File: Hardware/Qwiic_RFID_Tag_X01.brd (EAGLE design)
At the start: 112.5 x 103.6 mm, 294 parts, among them J1 Qwiic, J10 Qwiic, J11 Qwiic, J13 Qwiic, J14 Qwiic, J16 Qwiic, J17 Qwiic, J2 Qwiic, J4 Qwiic, J5 Qwiic, J7 Qwiic, J8 Qwiic, U1 ST25DV64KC, U2 ST25DV64KC, U3 ST25DV64KC, U4 ST25DV64KC, U5 ST25DV64KC, U6 ST25DV64KC

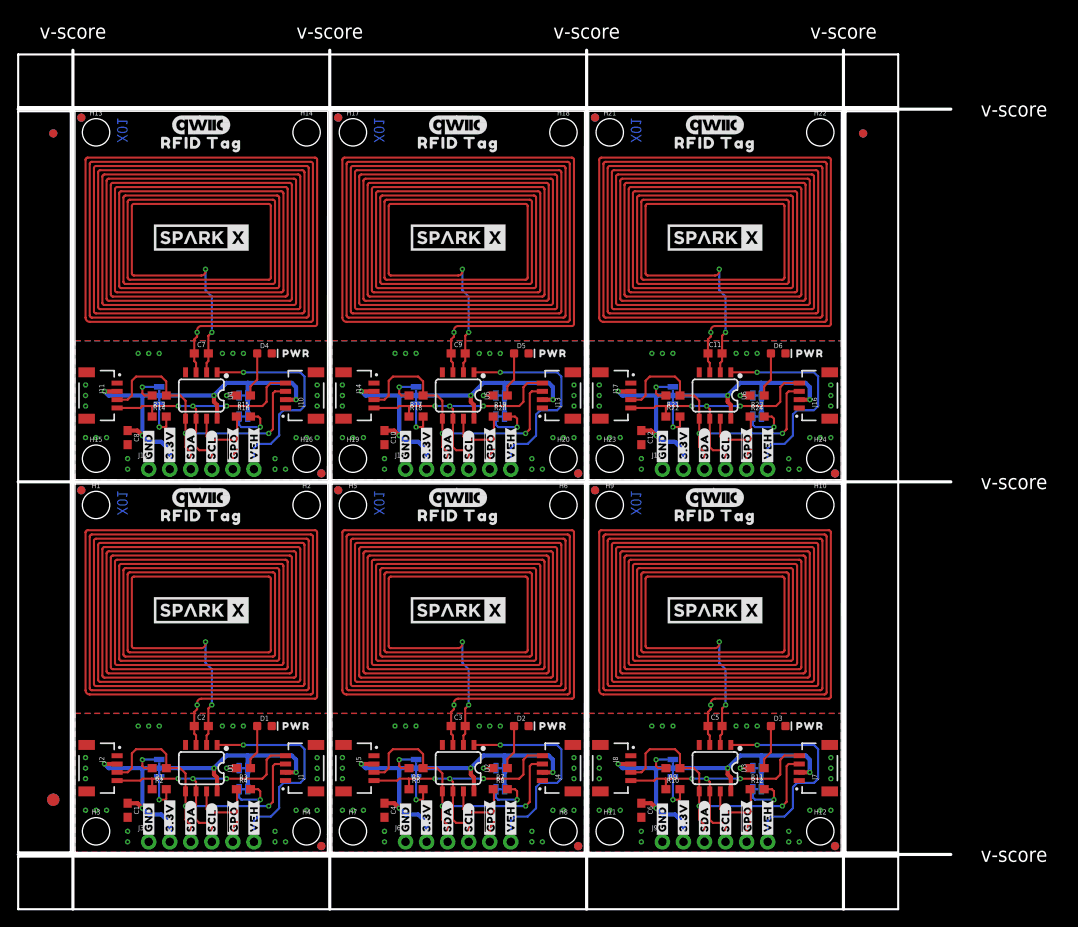
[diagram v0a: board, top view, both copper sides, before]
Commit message: Renamed file to reflect version. Added PCB version to bottom silk.
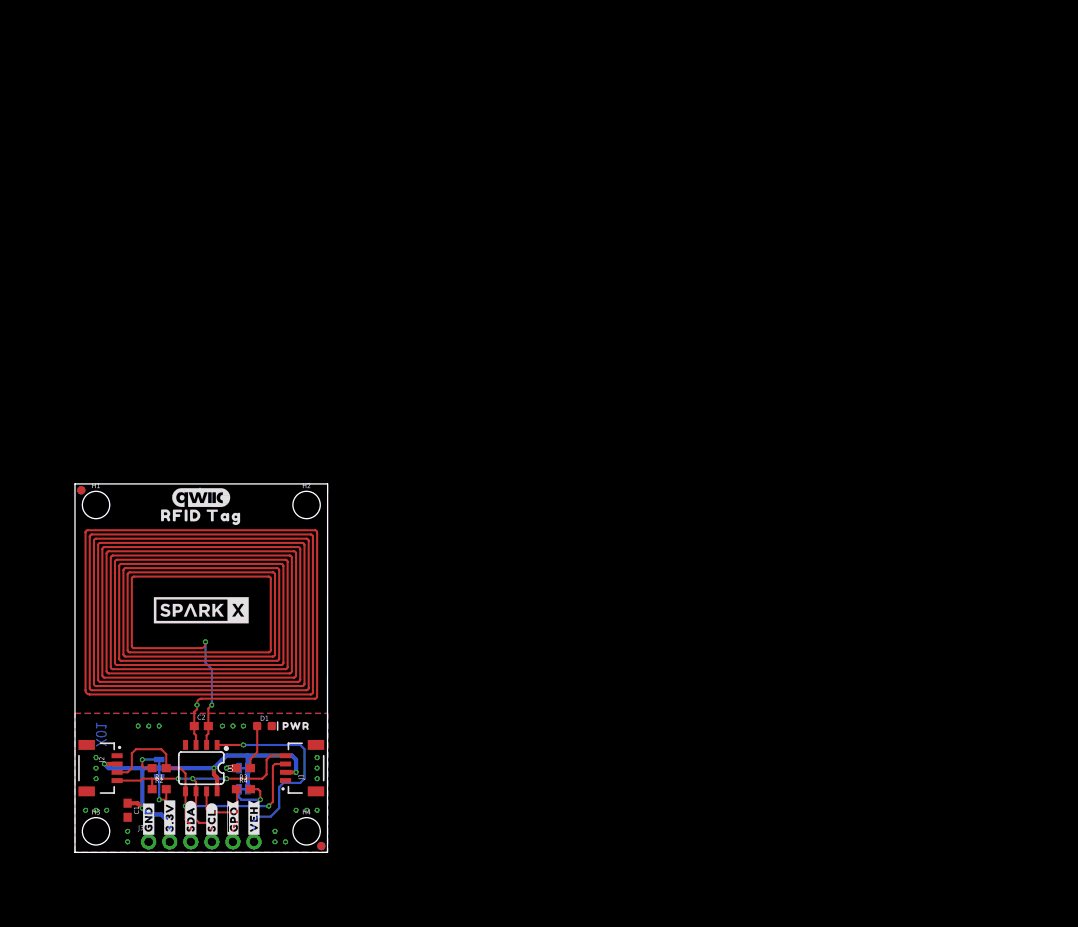
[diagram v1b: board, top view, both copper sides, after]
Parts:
- removed C10, C12, C4, C6, C8: 0.1uF, SparkFun-Capacitors:0603
- removed C11, C3, C5, C7, C9: 4.7pF, SparkFun-Capacitors:0603
- removed D2, D3, D4, D5, D6: RED, SparkFun-LED:LED-0603
- removed E$1, E$2, E$3, E$4: (no value), SparkFun-Aesthetics:FIDUCIAL-1X2
- removed E$5, E$6: (no value), SparkFun-Retired:FIDUCIAL-1.5X3
- removed FD10, FD11, FD12, FD13, FD14, FD15, FD16, FD17, FD18, FD19, FD20, FD21, FD22, FD23, FD24, FD5, FD6, FD7, FD8, FD9: FIDUCIAL1X2, SparkFun-Aesthetics:FIDUCIAL-1X2
- removed FRAME2, FRAME3, FRAME4, FRAME5, FRAME6: FRAME-LETTERNO_PACKAGE, SparkFun-Aesthetics:DUMMY
- removed H10, H11, H12, H13, H14, H15, H16, H17, H18, H19, H20, H21, H22, H23, H24, H5, H6, H7, H8, H9: STAND-OFF, SparkFun-Hardware:STAND-OFF
- removed J10, J11, J13, J14, J16, J17, J4, J5, J7, J8: Qwiic, SparkFun-Connectors:JST04_1MM_RA
- removed J12, J15, J18, J6, J9: (no value), SparkFun-Connectors:1X06_NO_SILK
- removed JP10, JP13, JP16, JP4, JP7: JUMPER-SMT_3_2-NC_TRACE_SILK, SparkFun-Jumpers:SMT-JUMPER_3_2-NC_TRACE_SILK
- removed JP11, JP12, JP14, JP15, JP17, JP18, JP5, JP6, JP8, JP9: JUMPER-SMT_2_NC_TRACE_SILK, SparkFun-Jumpers:SMT-JUMPER_2_NC_TRACE_SILK
- removed L2, L3, L4, L5, L6: PCB_4UH_INDUCTOR, SparkFun-Coils:PCB_4UH_INDUCTOR
- removed LOGO10, LOGO13, LOGO16, LOGO4, LOGO7: OSHW-LOGOMINI, SparkFun-Aesthetics:OSHW-LOGO-MINI
- removed LOGO11, LOGO12, LOGO14, LOGO15, LOGO17, LOGO18, LOGO5, LOGO6, LOGO8, LOGO9: QWIIC_LOGO_7MM, SparkFun-Aesthetics:QWIIC_7MM
- removed R10, R13, R14, R17, R18, R21, R22, R5, R6, R9: 2.2k, SparkFun-Resistors:0603
- removed R11, R15, R19, R23, R7: 1k, SparkFun-Resistors:0603
- removed R12, R16, R20, R24, R8: 10k, SparkFun-Resistors:0603
- removed U$100, U$110, U$121, U$26, U$37, U$47, U$58, U$68, U$79, U$89: (no value), output:#SDA#5
- removed U$101, U$111, U$122, U$27, U$38, U$48, U$59, U$69, U$80, U$90: (no value), output:#SCL#6
- removed U$102, U$112, U$123, U$28, U$39, U$49, U$60, U$70, U$81, U$91: (no value), output:##GPO##8
- removed U$103, U$113, U$124, U$29, U$40, U$50, U$61, U$71, U$82, U$92: (no value), output:#VEH#7
- removed U$104, U$105, U$125, U$126, U$41, U$42, U$62, U$63, U$83, U$84: (no value), output:RFID_TAG13
- removed U$106, U$107, U$13, U$43, U$44, U$64, U$65, U$85, U$86: SPARKX-LOGO5, SparkX:SPARKX-LARGE
- removed U$108, U$120, U$24, U$36, U$45, U$57, U$66, U$78, U$87, U$99: (no value), output:#3#3V#0
- removed U$109, U$119, U$25, U$35, U$46, U$56, U$67, U$77, U$88, U$98: (no value), output:#GND#4
- removed U$114, U$30, U$51, U$72, U$93: (no value), output:PWR11
- removed U$115, U$31, U$52, U$73, U$94: (no value), output:MADE_IN_THE_USA27
- removed U$116, U$32, U$53, U$74, U$95: (no value), output:#I2C#11
- removed U$117, U$33, U$54, U$75, U$96: (no value), output:##GPO##9
- removed U$118, U$34, U$55, U$76, U$97: (no value), output:#LED#10
- removed U2, U3, U4, U5, U6: ST25DV64KC, SparkFun-RF:SO08
- U$10: value SPARKX-LOGO5 -> (none); device SparkX:SPARKX-LARGE -> numbers:PCB#16329163281
- moved U$10 48.3 mm to (1.27, 11.7), flipped to the bottom, turned to 90 degrees
- moved LOGO1 27.0 mm to (28.7, 15.2)
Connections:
- removed net !GPO!1: J6.5, R8.1, U2.7
- removed net !GPO!2: J9.5, R12.1, U3.7
- removed net !GPO!3: J12.5, R16.1, U4.7
- removed net !GPO!4: J15.5, R20.1, U5.7
- removed net !GPO!5: J18.5, R24.1, U6.7
- removed net 3.3V1: C4.1, J4.2, J5.2, J6.2, JP4.2, JP5.2, JP6.2, U2.8
- removed net 3.3V2: C6.1, J7.2, J8.2, J9.2, JP7.2, JP8.2, JP9.2, U3.8
- removed net 3.3V3: C8.1, J10.2, J11.2, J12.2, JP10.2, JP11.2, JP12.2, U4.8
- removed net 3.3V4: C10.1, J13.2, J14.2, J15.2, JP13.2, JP14.2, JP15.2, U5.8
- removed net 3.3V5: C12.1, J16.2, J17.2, J18.2, JP16.2, JP17.2, JP18.2, U6.8
- removed net AC10: C11.2, L6.IN1, U6.2
- removed net AC11: C11.1, L6.IN2, U6.3
- removed net AC2: C3.2, L2.IN1, U2.2
- removed net AC3: C3.1, L2.IN2, U2.3
- removed net AC4: C5.2, L3.IN1, U3.2
- removed net AC5: C5.1, L3.IN2, U3.3
- removed net AC6: C7.2, L4.IN1, U4.2
- removed net AC7: C7.1, L4.IN2, U4.3
- removed net AC8: C9.2, L5.IN1, U5.2
- removed net AC9: C9.1, L5.IN2, U5.3
- removed net GND1: C4.2, D2.C, J4.1, J5.1, J6.1, U2.4
- removed net GND2: C6.2, D3.C, J7.1, J8.1, J9.1, U3.4
- removed net GND3: C8.2, D4.C, J10.1, J11.1, J12.1, U4.4
- removed net GND4: C10.2, D5.C, J13.1, J14.1, J15.1, U5.4
- removed net GND5: C12.2, D6.C, J16.1, J17.1, J18.1, U6.4
- removed net N$10: JP6.1, R8.2
- removed net N$11: JP7.3, R9.2
- removed net N$12: JP7.1, R10.2
- removed net N$13: JP8.1, R11.2
- removed net N$14: D3.A, R11.1
- removed net N$15: JP9.1, R12.2
- removed net N$16: JP10.3, R13.2
- removed net N$17: JP10.1, R14.2
- removed net N$18: JP11.1, R15.2
- removed net N$19: D4.A, R15.1
- removed net N$20: JP12.1, R16.2
- removed net N$21: JP13.3, R17.2
- removed net N$22: JP13.1, R18.2
- removed net N$23: JP14.1, R19.2
- removed net N$24: D5.A, R19.1
- removed net N$25: JP15.1, R20.2
- removed net N$26: JP16.3, R21.2
- removed net N$27: JP16.1, R22.2
- removed net N$28: JP17.1, R23.2
- removed net N$29: D6.A, R23.1
- removed net N$30: JP18.1, R24.2
- removed net N$6: JP4.3, R5.2
- removed net N$7: JP4.1, R6.2
- removed net N$8: JP5.1, R7.2
- removed net N$9: D2.A, R7.1
- removed net SCL1: J4.4, J5.4, J6.4, R6.1, U2.6
- removed net SCL2: J7.4, J8.4, J9.4, R10.1, U3.6
- removed net SCL3: J10.4, J11.4, J12.4, R14.1, U4.6
- removed net SCL4: J13.4, J14.4, J15.4, R18.1, U5.6
- removed net SCL5: J16.4, J17.4, J18.4, R22.1, U6.6
- removed net SDA1: J4.3, J5.3, J6.3, R5.1, U2.5
- removed net SDA2: J7.3, J8.3, J9.3, R9.1, U3.5
- removed net SDA3: J10.3, J11.3, J12.3, R13.1, U4.5
- removed net SDA4: J13.3, J14.3, J15.3, R17.1, U5.5
- removed net SDA5: J16.3, J17.3, J18.3, R21.1, U6.5
- removed net VEH1: J6.6, U2.1
- removed net VEH2: J9.6, U3.1
- removed net VEH3: J12.6, U4.1
- removed net VEH4: J15.6, U5.1
- removed net VEH5: J18.6, U6.1
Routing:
- net 3.3V5: track 48.7 -> 0.00 mm, vias 4 -> 0
- net 3.3V4: track 48.7 -> 0.00 mm, vias 4 -> 0
- net 3.3V3: track 48.7 -> 0.00 mm, vias 4 -> 0
- net 3.3V2: track 48.7 -> 0.00 mm, vias 4 -> 0
- net 3.3V1: track 48.7 -> 0.00 mm, vias 4 -> 0
- net SDA4: track 37.9 -> 0.00 mm, vias 2 -> 0
- net SDA3: track 37.9 -> 0.00 mm, vias 2 -> 0
- net SDA5: track 37.9 -> 0.00 mm, vias 2 -> 0
- net SDA2: track 37.9 -> 0.00 mm, vias 2 -> 0
- net SDA1: track 37.9 -> 0.00 mm, vias 2 -> 0
- net SCL2: track 33.1 -> 0.00 mm, vias 3 -> 0
- net SCL1: track 33.1 -> 0.00 mm, vias 3 -> 0
- net SCL5: track 33.1 -> 0.00 mm, vias 3 -> 0
- net SCL3: track 33.1 -> 0.00 mm, vias 3 -> 0
- net SCL4: track 33.1 -> 0.00 mm, vias 3 -> 0
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- removed copper zone on layer 1, net GND1
- removed copper zone on layer 16, net GND1
- removed copper zone on layer 1, net GND2
- removed copper zone on layer 16, net GND2
- removed copper zone on layer 1, net GND3
- removed copper zone on layer 16, net GND3
- removed copper zone on layer 1, net GND4
- removed copper zone on layer 16, net GND4
- removed copper zone on layer 1, net GND5
- removed copper zone on layer 16, net GND5
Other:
- board size 112.5 x 103.6 mm -> 30.5 x 44.5 mm
- board text added: "Dimensions in inches"
- board text removed: "v-score"

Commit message: Added production files; updated BOM.
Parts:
- removed U$10: (no value), numbers:PCB#16329163281
- removed U$14: (no value), output:MADE_IN_THE_USA27
- added U$13, U$24: (no value), SER:ST25DV64KC5984
- added U$34: (no value), output:MADE_IN_THE_USA20
- moved U$2 13.5 mm to (15.2, 28.4)
- moved U$12 11.9 mm to (15.2, 40.6)
- moved LOGO3 11.4 mm to (15.2, 31.4)
- moved U$1 1.02 mm to (15.2, 28.2)
- moved LOGO2 0.25 mm to (15.2, 31.6)
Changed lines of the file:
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@@
 <setting verticaltext="up"/>
 </settings>
-<grid distance="0.05" unitdist="inch" unit="inch" style="lines" multiple="1" display="yes" altdistance="0.005" altunitdist="inch" altunit="inch"/>
+<grid distance="0.01" unitdist="inch" unit="inch" style="lines" multiple="1" display="yes" altdistance="0.005" altunitdist="inch" altunit="inch"/>
 <layers>
 <layer number="1" name="Top" color="4" fill="1" visible="yes" active="yes"/>
@@
 <wire x1="30.48" y1="44.45" x2="0" y2="44.45" width="0" layer="20"/>
 <wire x1="0" y1="44.45" x2="0" y2="0" width="0" layer="20"/>
-<text x="2.54" y="12.7" size="1.27" layer="16" font="vector" ratio="15" rot="MR90">X01</text>
+<text x="1.778" y="13.462" size="1.27" layer="16" font="vector" ratio="15" rot="MR90">X01</text>
 <dimension x1="0" y1="-1.27" x2="30.48" y2="-1.27" x3="15.24" y3="-3.81" textsize="1.778" layer="47" dtype="horizontal" unit="inch"/>
 <dimension x1="-1.27" y1="44.45" x2="-1.27" y2="0" x3="-2.54" y3="22.225" textsize="1.778" layer="47" dtype="vertical" unit="inch"/>
@@
 <element name="FD4" library="SparkFun-Aesthetics" package="FIDUCIAL-1X2" value="FIDUCIAL1X2" x="29.718" y="0.762" smashed="yes"/>
 <element name="LOGO1" library="SparkFun-Aesthetics" package="OSHW-LOGO-MINI" value="OSHW-LOGOMINI" x="28.702" y="15.24" smashed="yes" rot="MR0"/>
-<element name="LOGO3" library="SparkFun-Aesthetics" package="QWIIC_7MM" value="QWIIC_LOGO_7MM" x="15.24" y="42.799" smashed="yes"/>
+<element name="LOGO3" library="SparkFun-Aesthetics" package="QWIIC_7MM" value="QWIIC_LOGO_7MM" x="15.24" y="31.369" smashed="yes"/>
 <element name="H1" library="SparkFun-Hardware" package="STAND-OFF" value="STAND-OFF" x="2.54" y="41.91" smashed="yes">
 <attribute name="NAME" x="2.54" y="43.942" size="0.6096" layer="25" font="vector" ratio="20" align="bottom-center"/>
@@
 <attribute name="VALUE" x="27.94" y="0.508" size="0.6096" layer="27" font="vector" ratio="20" align="top-center"/>
 </element>
-<element name="U$1" library="SparkX" package="SPARKX-LARGE" value="SPARKX-LOGO5" x="15.24" y="29.21" smashed="yes"/>
-<element name="U$2" library="SparkX" package="SPARKX-LARGE" value="SPARKX-LOGO5" x="15.24" y="41.91" smashed="yes" rot="MR0"/>
+<element name="U$1" library="SparkX" package="SPARKX-LARGE" value="SPARKX-LOGO5" x="15.24" y="28.194" smashed="yes"/>
+<element name="U$2" library="SparkX" package="SPARKX-LARGE" value="SPARKX-LOGO5" x="15.24" y="28.448" smashed="yes" rot="MR0"/>
 <element name="U$3" library="output" package="#3#3V#0" value="" x="11.43" y="1.778" smashed="yes" rot="R90"/>
 <element name="U$4" library="output" package="#GND#4" value="" x="8.89" y="1.778" smashed="yes" rot="R90"/>
@@
 <element name="U$8" library="output" package="#VEH#7" value="" x="21.59" y="1.778" smashed="yes" rot="R90"/>
 <element name="U$9" library="output" package="PWR11" value="" x="26.67" y="15.24" smashed="yes"/>
-<element name="U$14" library="output" package="MADE_IN_THE_USA27" value="" x="15.24" y="26.67" smashed="yes" rot="MR0"/>
 <element name="U$15" library="output" package="#I2C#11" value="" x="10.16" y="12.7" smashed="yes" rot="MR0"/>
 <element name="U$16" library="output" package="##GPO##9" value="" x="21.336" y="7.62" smashed="yes" rot="MR0"/>
@@
 <element name="U$23" library="output" package="#VEH#7" value="" x="21.59" y="1.778" smashed="yes" rot="MR90"/>
 <element name="U$11" library="output" package="RFID_TAG13" value="" x="15.24" y="40.64" smashed="yes"/>
-<element name="U$12" library="output" package="RFID_TAG13" value="" x="15.24" y="28.702" smashed="yes" rot="MR0"/>
-<element name="LOGO2" library="SparkFun-Aesthetics" package="QWIIC_7MM" value="QWIIC_LOGO_7MM" x="15.24" y="31.369" smashed="yes" rot="MR0"/>
-<element name="U$10" library="numbers" package="PCB#16329163281" value="" x="1.27" y="11.684" smashed="yes" rot="MR90"/>
+<element name="U$12" library="output" package="RFID_TAG13" value="" x="15.24" y="40.64" smashed="yes" rot="MR0"/>
+<element name="LOGO2" library="SparkFun-Aesthetics" package="QWIIC_7MM" value="QWIIC_LOGO_7MM" x="15.24" y="31.623" smashed="yes" rot="MR0"/>
+<element name="U$13" library="SER" package="ST25DV64KC5984" value="" x="15.24" y="42.672" smashed="yes"/>
+<element name="U$24" library="SER" package="ST25DV64KC5984" value="" x="15.24" y="42.672" smashed="yes" rot="MR0"/>
+<element name="U$34" library="output" package="MADE_IN_THE_USA20" value="" x="0.762" y="11.684" smashed="yes" rot="MR90"/>
 </elements>
 <signals>
